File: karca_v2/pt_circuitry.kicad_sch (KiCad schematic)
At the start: 12 parts, among them U10 TLV9304xD, U9 TLV9304xD

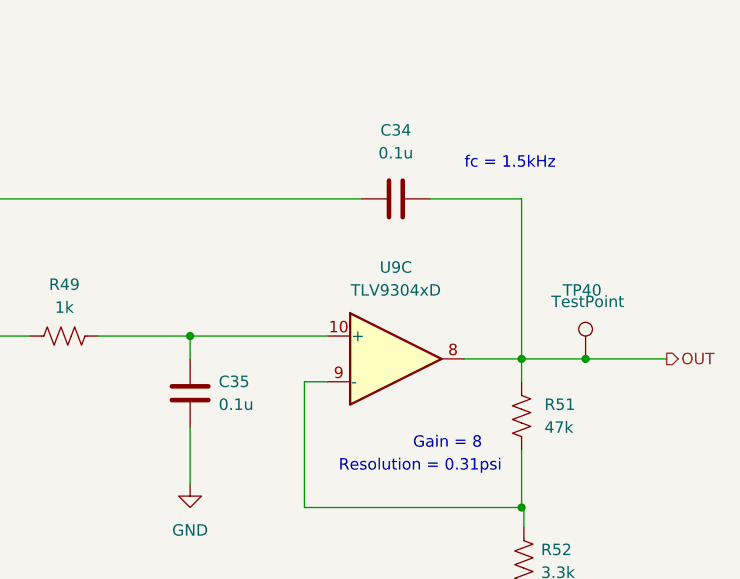
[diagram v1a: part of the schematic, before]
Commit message: finished schematic for v2.1
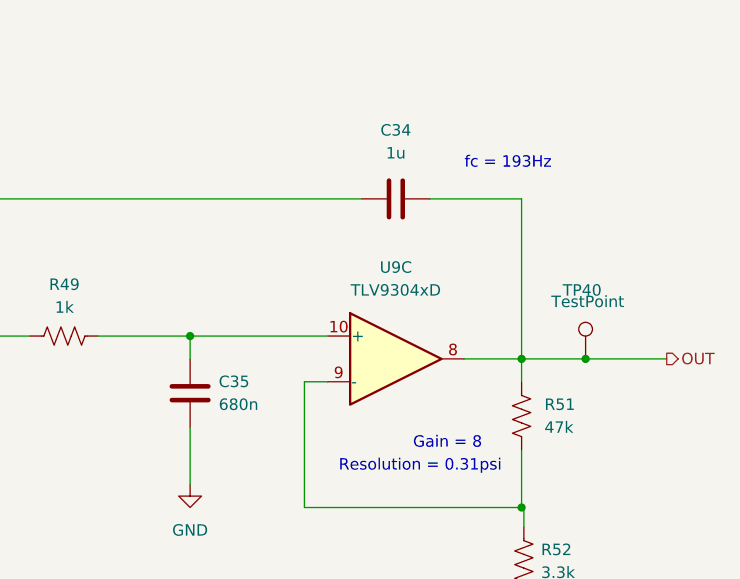
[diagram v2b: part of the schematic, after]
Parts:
- C34: value 0.1u -> 1u
- C35: value 0.1u -> 680n
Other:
- note added: "fc = 193Hz"
- note removed: "fc = 1.5kHz"
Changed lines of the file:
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@@
 		)
 	)
-	(text "fc = 1.5kHz\n"
+	(text "fc = 193Hz\n"
 		(exclude_from_sim no)
 		(at 199.136 54.991 0)
@@
 			)
 		)
-		(property "Value" "0.1u"
+		(property "Value" "1u"
 			(at 191.516 53.086 90)
 			(effects
@@
 			)
 		)
-		(property "Value" "0.1u"
+		(property "Value" "680n"
 			(at 171.831 81.026 0)
 			(effects
